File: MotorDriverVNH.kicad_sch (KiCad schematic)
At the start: 4 parts, among them IC1 VNH7070ASTR, J1 Conn_01x02, J3 Conn_01x05

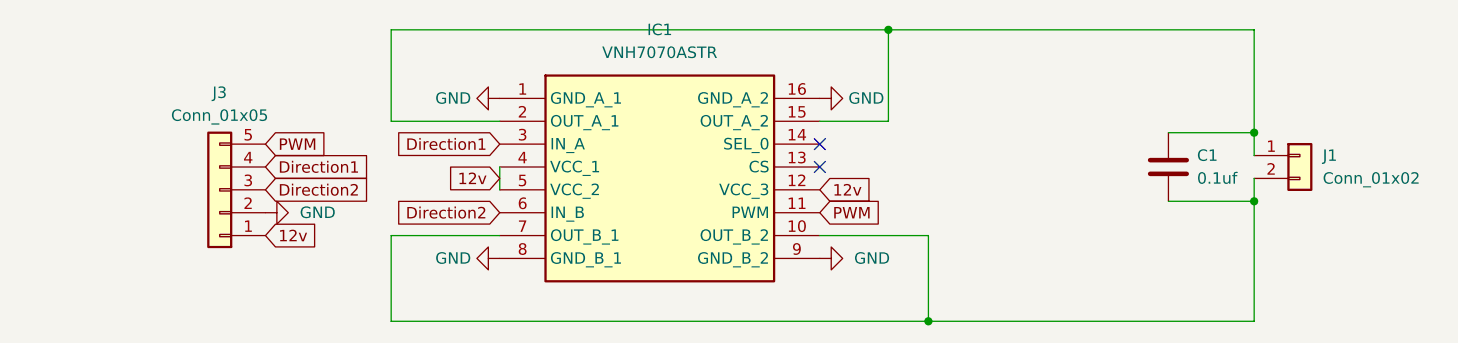
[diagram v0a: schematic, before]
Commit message: Added Resistors
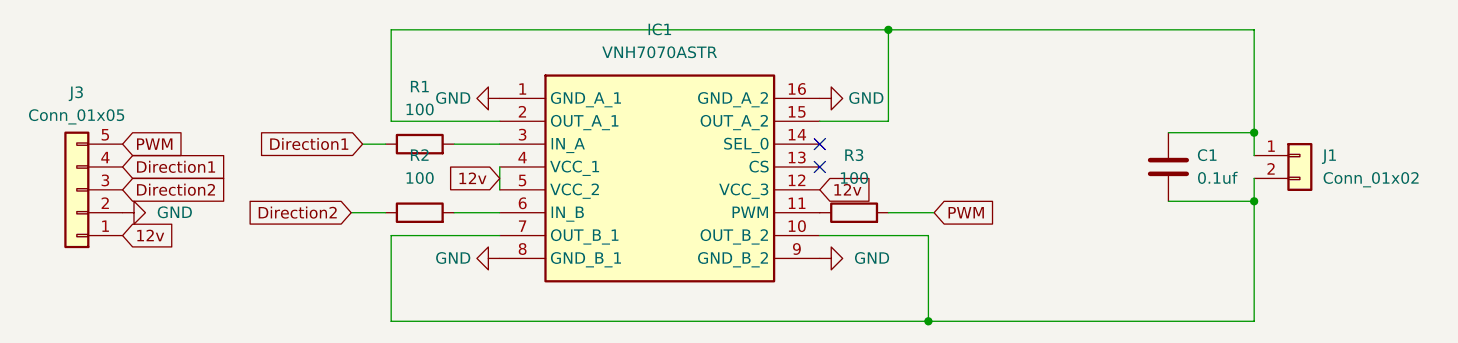
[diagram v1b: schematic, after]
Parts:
- added R1, R2, R3: 100, Resistor_SMD:R_0805_2012Metric_Pad1.20x1.40mm_HandSolder, symbol Device:R
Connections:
- net Direction1: now also R1.1; no longer IC1.3 (IN_A)
- net Direction2: now also R2.1; no longer IC1.6 (IN_B)
- net PWM: now also R3.2; no longer IC1.11 (PWM)
- new net: IC1.6 (IN_B), R2.2
- new net: IC1.11 (PWM), R3.1
- new net: IC1.3 (IN_A), R1.2
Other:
- moved on the sheet: J3
